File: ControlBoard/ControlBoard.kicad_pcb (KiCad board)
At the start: 2 copper layers, 144 x 106 mm, 194 parts, among them J1 PowerIn, J10 Conn_01x01, J11 Conn_01x01, J12 Conn_01x01, J13 Conn_01x01, J14 Conn_01x01, J15 Conn_01x01, J16 Conn_01x06, J17 Conn_01x06, J18 Conn_01x06, J19 HALLSENS, J2 UART, J20 Conn_01x06, J21 HALLSENS2, J22 PowerIn, J3 ICSP, J4 MTR1, J5 MTR2, J6 Ultrasonic Transmitter, J7 Ultrasonic Receiver, J8 Conn_01x01, J9 Conn_01x01, Q1 2N3904, Q2 2N3904, SW1 SW_Push, U1 LM358, U10 LMT85, U11 74HC138, U12 4051, U13 4051, U14 74HC14, U2 LM358, U3 LM358, U4 LM358, U5 ATMEGA328P-PU, U6 LM7805_TO220, U7 74HC595, U8 L298D, U9 74HC595, Y1 16MHz

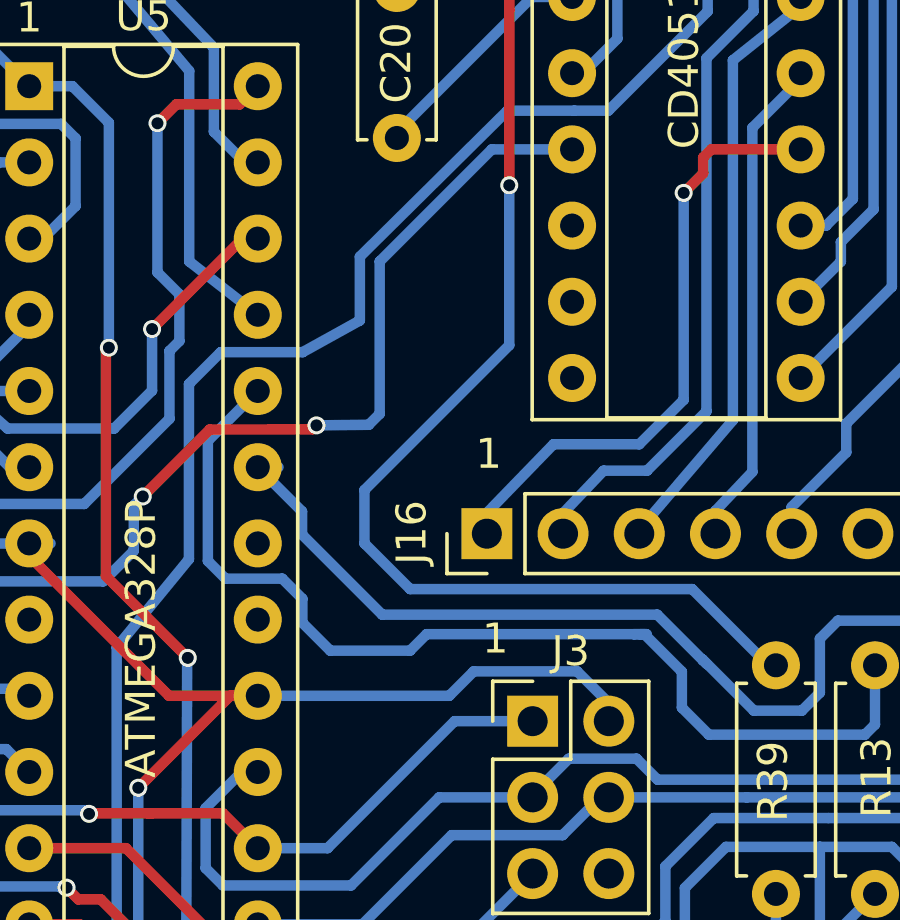
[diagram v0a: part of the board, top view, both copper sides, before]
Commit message: Added capacitor for AREF
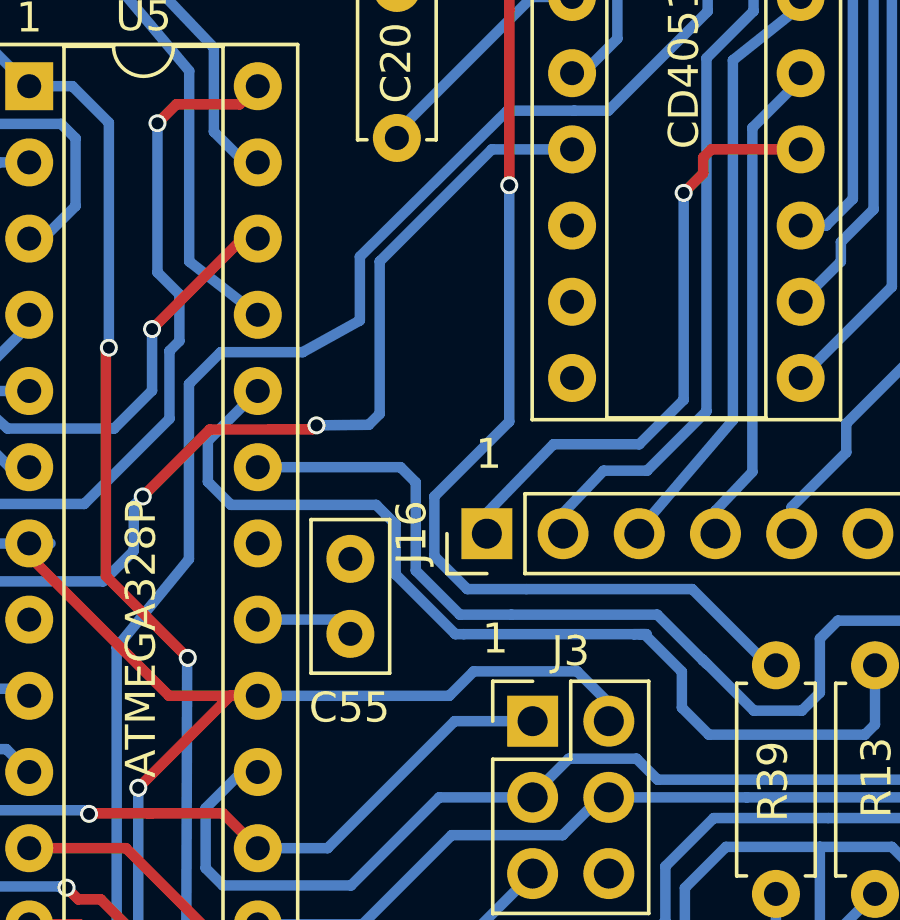
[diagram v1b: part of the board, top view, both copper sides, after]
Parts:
- added C55: 100 nF, Capacitors_THT:C_Disc_D5.0mm_W2.5mm_P2.50mm, F.Cu at (146.8, 106.1)
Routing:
- net Net-(C55-Pad1): track 0.00 -> 3.28 mm
- net Net-(R39-Pad2): track 62.6 -> 59.6 mm
- net CURSEN2: track 35.5 -> 34.0 mm
- net CURSEN1: track 39.9 -> 41.2 mm

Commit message: new commit
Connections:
- U9 pad 15: Net-(U9-Pad15) -> unconnected-(U9-QA-Pad15)
- U9 pad 9: Net-(U9-Pad9) -> unconnected-(U9-~{QH}-Pad9)
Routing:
- net +5V: track 1089.6 -> 1074.9 mm
- net Net-(ID3-K): track 86.8 -> 83.5 mm
- net CURSEN1: track 41.2 -> 38.4 mm
- net Net-(J7-Pin_2): track 15.3 -> 13.3 mm
- net SCK: track 69.4 -> 67.5 mm
- net MTRIN2: track 19.1 -> 17.3 mm
- net Net-(J6-Pin_1): track 34.7 -> 32.9 mm
- net Net-(ID1-K): track 11.7 -> 9.91 mm
- net Net-(PT2-C): track 125.0 -> 123.4 mm
- net Net-(PDT4-E): track 33.0 -> 31.4 mm
- net Net-(U7-~{QH}): track 21.2 -> 19.6 mm
- net MTRIN1: track 16.4 -> 15.1 mm
- net Net-(PDT2-E): track 113.1 -> 111.9 mm
- net 2V5: track 326.4 -> 325.3 mm
- net Net-(PT4-C): track 79.9 -> 78.9 mm
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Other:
- net class Default removed
